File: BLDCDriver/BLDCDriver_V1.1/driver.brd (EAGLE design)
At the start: 160 x 100 mm, 70 parts, among them Q2 SIZ240DT-T1-GE3, Q3 SIZ240DT-T1-GE3, Q4 SIZ240DT-T1-GE3, U1 QFN50P400X400X100-25NDRV8300D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, U4 SOP80P620X125-8N, X2 JST-XH-06-PIN-LONG-PAD

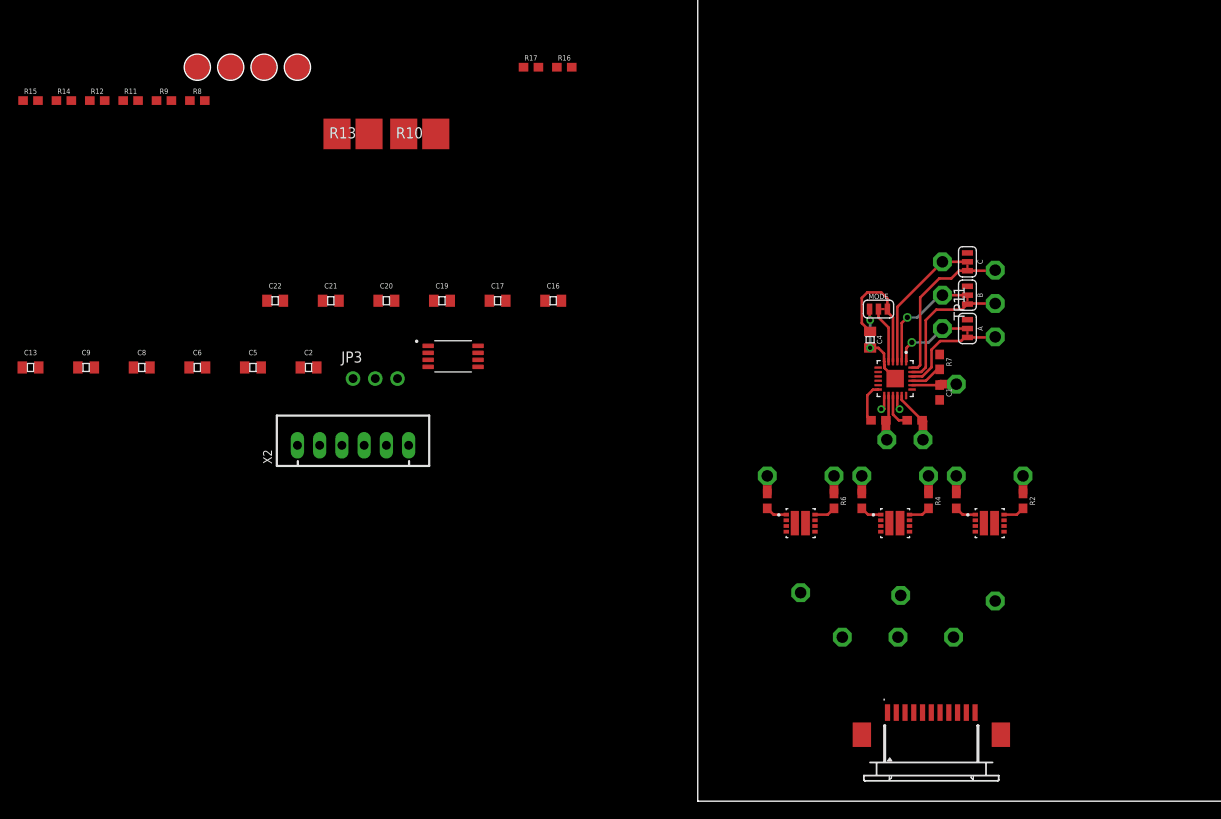
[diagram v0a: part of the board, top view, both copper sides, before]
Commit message: fix position BST condenser
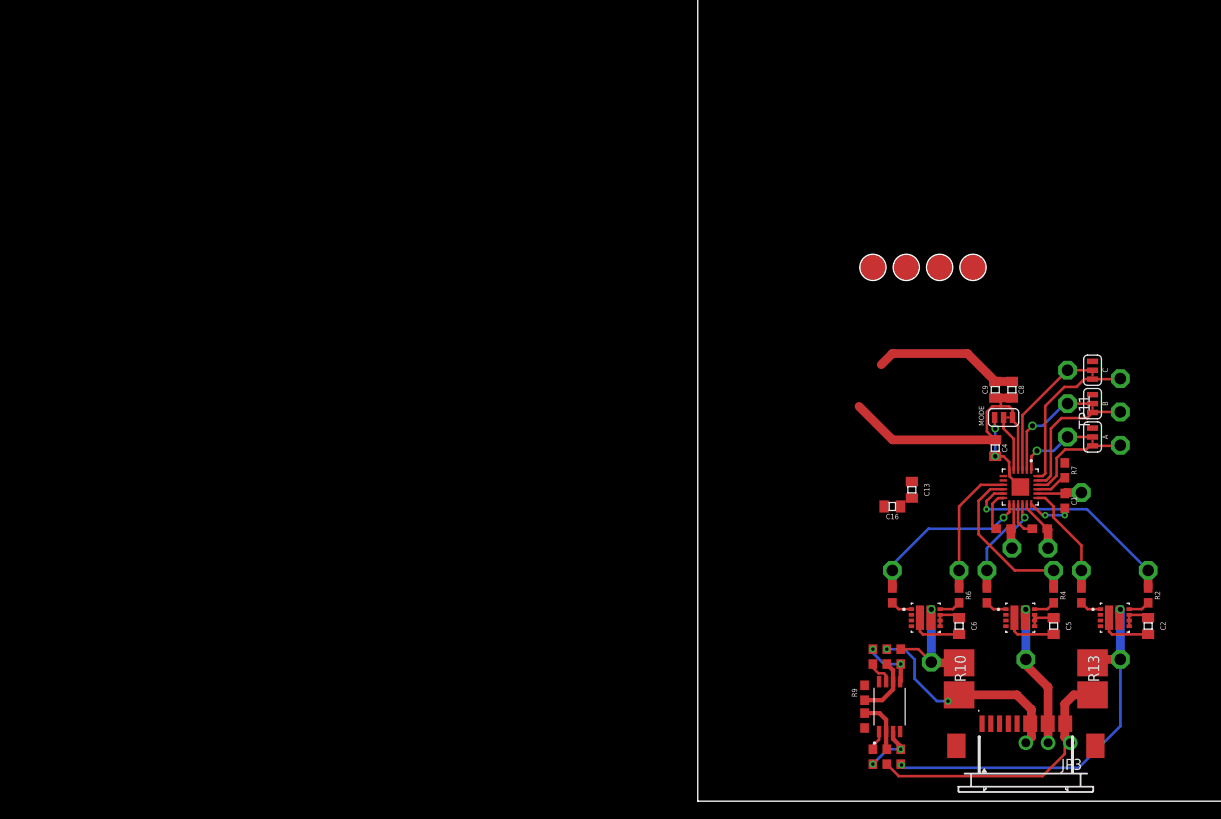
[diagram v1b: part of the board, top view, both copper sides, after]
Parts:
- removed C17, C19, C20, C21, C22: 22UF-1210, capsmd:0805
- removed TP22, TP23, TP24: TPPAD1-13, testpad:P1-13
- removed X2: JST-XH-06-PIN-LONG-PAD, Rembrandt Electronics - JST XH Connectors v1-0:JST-XH-06-PACKAGE-LONG-PAD
- moved R15 123.2 mm to (21.6, 5.08), turned to 270 degrees
- moved R14 121.4 mm to (23.2, 5.08), turned to 270 degrees
- moved R12 110.3 mm to (21.6, 16.5), turned to 90 degrees
- moved R11 108.5 mm to (23.2, 16.5), turned to 90 degrees
- moved R13 104.9 mm to (45.1, 14.0), turned to 270 degrees
- moved R9 104.8 mm to (19.1, 12.4), turned to 270 degrees
- moved C9 103.9 mm to (34.0, 47.0), turned to 270 degrees
- moved C13 101.6 mm to (24.4, 35.6), turned to 270 degrees
- moved C2 100.3 mm to (51.4, 20.0), turned to 270 degrees
- moved R8 99.9 mm to (20.0, 16.5), turned to 90 degrees
- moved C8 99.4 mm to (35.9, 47.0), turned to 270 degrees
- moved C5 96.1 mm to (40.6, 20.0), turned to 270 degrees
- moved C6 91.9 mm to (29.8, 20.0), turned to 270 degrees
- moved R10 87.6 mm to (29.8, 14.0), turned to 270 degrees
- moved JP3 87.4 mm to (40.0, 6.67), turned to 180 degrees
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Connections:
- removed net 5V: X2.4
- removed net CANH: X2.5
- removed net CANL: X2.6
- removed net GVDD_IN: X2.1
- net GND: no longer C17.1, C19.1, C20.1, C21.1, C22.1, X2.3
- net GVDD: no longer X2.2
- net PVDD: no longer C17.2, C19.2, C20.2, C21.2, C22.2
- net U: no longer TP24.TP
- net U_CS: now also ..10, ..11; no longer ..6, ..7
- net V: no longer TP23.TP
- net W: no longer TP22.TP
- net W_CS: now also ..6, ..7; no longer ..10, ..11
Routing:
- net U: track 0.00 -> 50.9 mm, vias 0 -> 4
- net U_CS: track 0.00 -> 34.7 mm
- net GND: track 9.70 -> 37.2 mm
- net W_CS: track 0.00 -> 26.3 mm, vias 0 -> 2
- net GLA: track 2.01 -> 26.6 mm, vias 0 -> 1
- net GVDD: track 15.2 -> 34.1 mm
- net PVDD: track 0.00 -> 18.5 mm
- net V: track 4.06 -> 22.3 mm, vias 0 -> 1
- net GLB: track 2.01 -> 19.5 mm
- net GHC: track 3.89 -> 19.4 mm
- net W: track 4.54 -> 19.0 mm, vias 0 -> 1
- net GLC: track 2.01 -> 15.4 mm
- net GHA: track 2.01 -> 12.9 mm
- net GHB: track 3.67 -> 12.0 mm
- net N$9: track 0.00 -> 6.95 mm
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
